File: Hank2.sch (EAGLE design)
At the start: 98 parts, among them T1 2n2222, T2 2n2222, T3 2n2222, T4 2n2222, T5 2n2222, T6 2n2222, T7 2n2222, T8 2n2222, X3 Auto_Manual

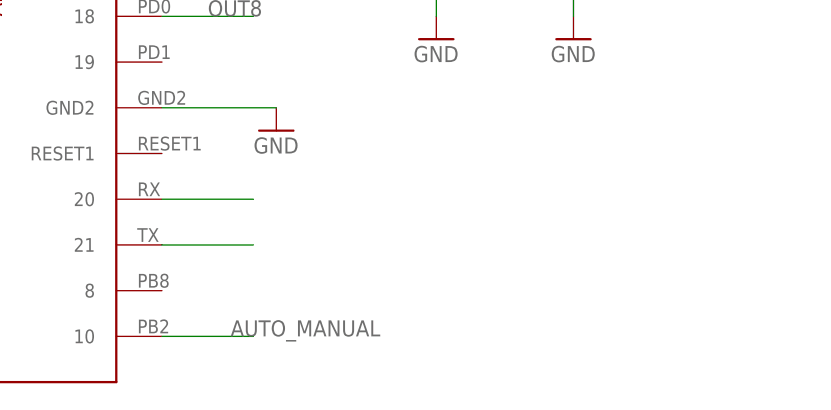
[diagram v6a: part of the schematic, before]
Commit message: Adding Arduino Serial communication and tiding up code
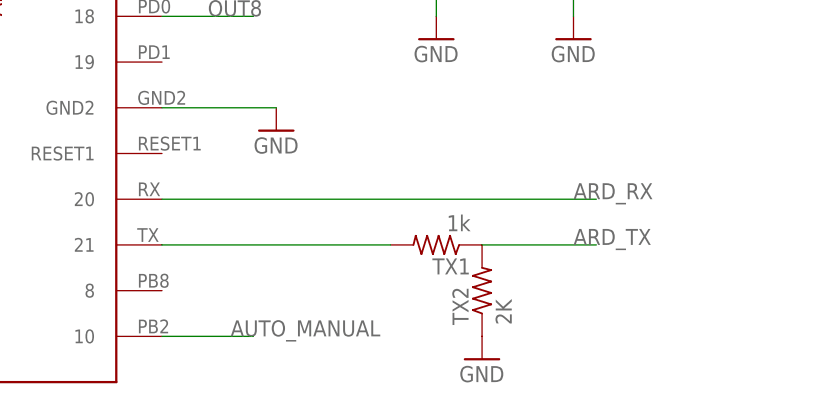
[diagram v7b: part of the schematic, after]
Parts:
- added TX1: 1k, rcl:R-US_0204/7
- added TX2: 2K, rcl:R-US_0204/7
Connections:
- net N$35 renamed ARD_RX
- new net ARD_TX: TX1.1, TX2.2
- net GND: now also TX2.1
- net N$6: now also TX1.2
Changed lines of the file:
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@@
 <part name="RO32" library="rcl" deviceset="R-US_" device="0204/7" value="10K"/>
 <part name="RO22" library="rcl" deviceset="R-US_" device="0204/7" value="10K"/>
+<part name="TX2" library="rcl" deviceset="R-US_" device="0204/7" value="2K"/>
+<part name="TX1" library="rcl" deviceset="R-US_" device="0204/7" value="1k"/>
+<part name="GND29" library="SparkFun" deviceset="GND" device=""/>
 </parts>
 <sheets>
@@
 <instance part="RO32" gate="G$1" x="200.66" y="114.3" rot="R180"/>
 <instance part="RO22" gate="G$1" x="200.66" y="167.64" rot="R180"/>
+<instance part="TX2" gate="G$1" x="200.66" y="17.78" rot="R90"/>
+<instance part="TX1" gate="G$1" x="195.58" y="22.86" rot="R180"/>
+<instance part="GND29" gate="1" x="200.66" y="10.16" smashed="yes">
+<attribute name="VALUE" x="198.12" y="7.62" size="1.778" layer="96"/>
+</instance>
 </instances>
 <busses>
@@
 <pinref part="GND3" gate="1" pin="GND"/>
 <wire x1="165.1" y1="38.1" x2="177.8" y2="38.1" width="0.1524" layer="91"/>
+</segment>
+<segment>
+<pinref part="TX2" gate="G$1" pin="1"/>
+<pinref part="GND29" gate="1" pin="GND"/>
 </segment>
 </net>
@@
 </segment>
 </net>
-<net name="N$6" class="0">
-<segment>
-<pinref part="ARDUINO" gate="G$1" pin="21"/>
-<wire x1="165.1" y1="22.86" x2="175.26" y2="22.86" width="0.1524" layer="91"/>
-</segment>
-</net>
-<net name="N$35" class="0">
+<net name="ARD_RX" class="0">
 <segment>
 <pinref part="ARDUINO" gate="G$1" pin="20"/>
-<wire x1="165.1" y1="27.94" x2="175.26" y2="27.94" width="0.1524" layer="91"/>
+<wire x1="165.1" y1="27.94" x2="213.36" y2="27.94" width="0.1524" layer="91"/>
+<label x="210.82" y="27.94" size="1.778" layer="95"/>
 </segment>
 </net>
@@
 </segment>
 </net>
+<net name="ARD_TX" class="0">
+<segment>
+<pinref part="TX2" gate="G$1" pin="2"/>
+<pinref part="TX1" gate="G$1" pin="1"/>
+<wire x1="200.66" y1="22.86" x2="213.36" y2="22.86" width="0.1524" layer="91"/>
+<label x="210.82" y="22.86" size="1.778" layer="95"/>
+</segment>
+</net>
+<net name="N$6" class="0">
+<segment>
+<pinref part="ARDUINO" gate="G$1" pin="21"/>
+<pinref part="TX1" gate="G$1" pin="2"/>
+<wire x1="165.1" y1="22.86" x2="190.5" y2="22.86" width="0.1524" layer="91"/>
+</segment>
+</net>
